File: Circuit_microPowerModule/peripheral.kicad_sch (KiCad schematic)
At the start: 25 parts, among them J4 Conn_01x08_Pin, J6 MikroBus

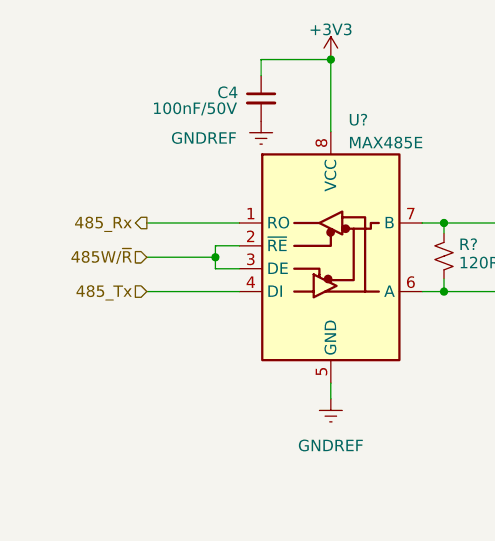
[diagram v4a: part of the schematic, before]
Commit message: define mcu pinout to mikrobus
update hw block diagram file type
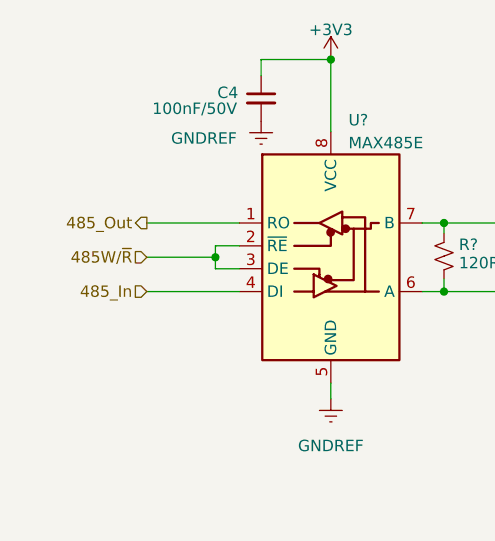
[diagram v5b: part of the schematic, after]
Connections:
- net 485_Rx renamed 485_Out
- net 485_Tx renamed 485_In
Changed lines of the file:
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@@
     (effects (font (size 1.27 1.27)) (justify right))
   )
-  (hierarchical_label "485_Tx" (shape input) (at 37.084 53.213 180) (fields_autoplaced)
+  (hierarchical_label "485_In" (shape input) (at 37.084 53.213 180) (fields_autoplaced)
     (effects (font (size 1.27 1.27)) (justify right))
   )
@@
     (effects (font (size 1.27 1.27)) (justify left))
   )
-  (hierarchical_label "485_Rx" (shape output) (at 37.084 45.593 180) (fields_autoplaced)
+  (hierarchical_label "485_Out" (shape output) (at 37.084 45.593 180) (fields_autoplaced)
     (effects (font (size 1.27 1.27)) (justify right))
   )

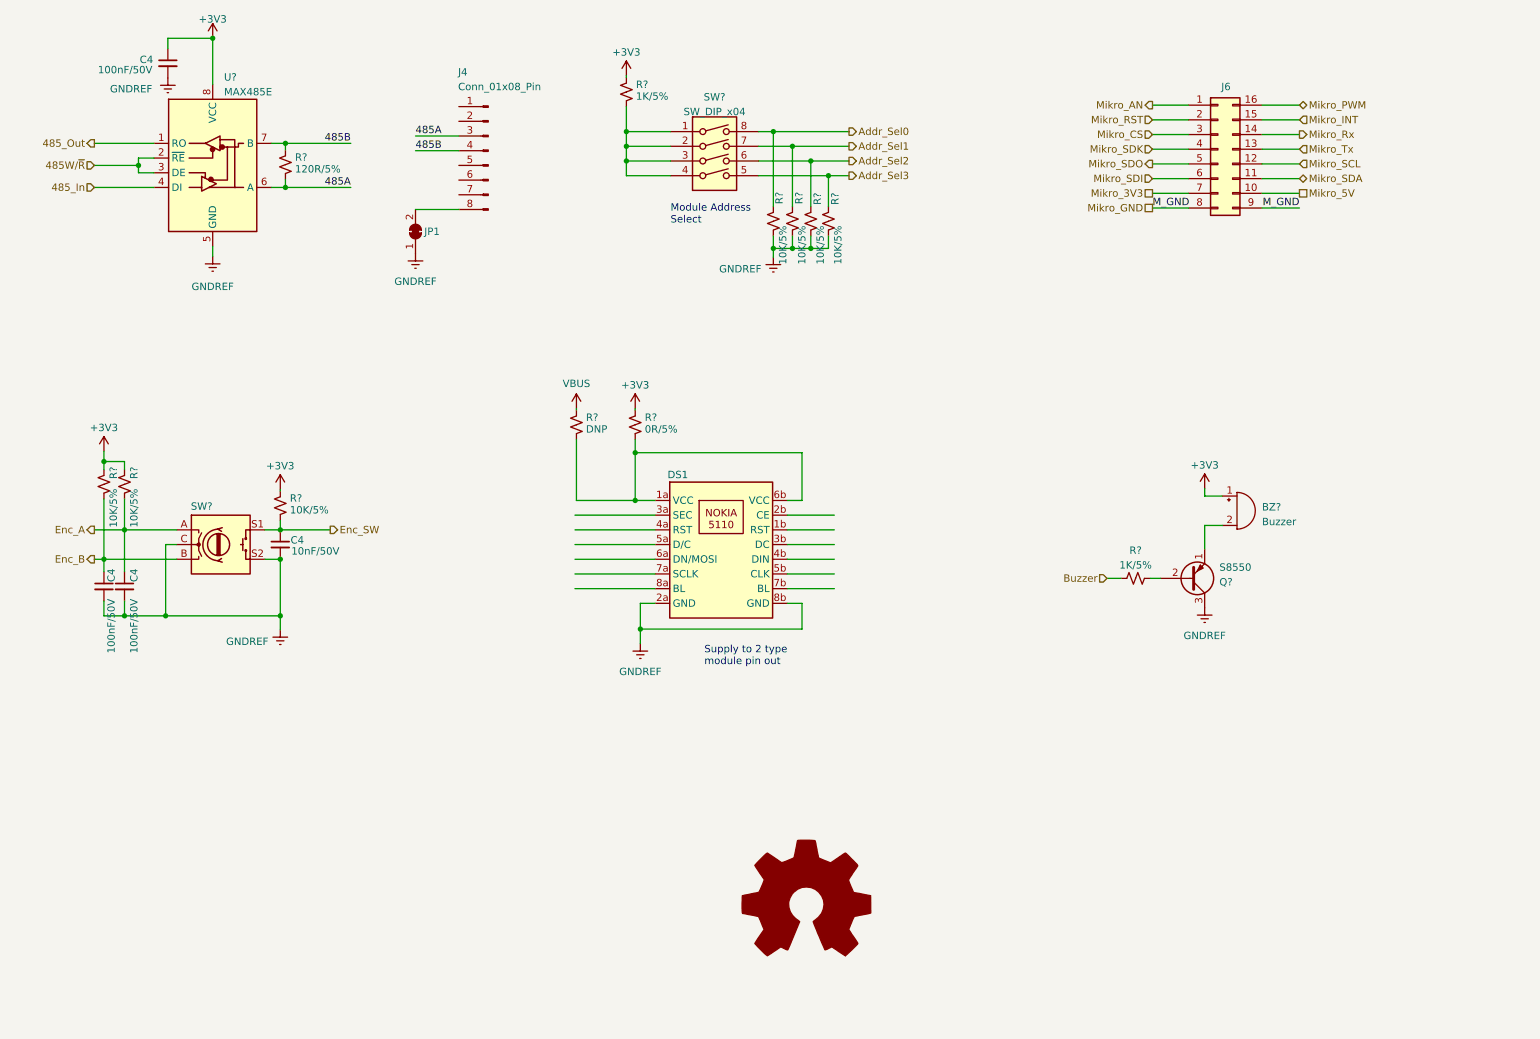
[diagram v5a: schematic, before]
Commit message: Completed microcontroller unit pin planning
update schematic
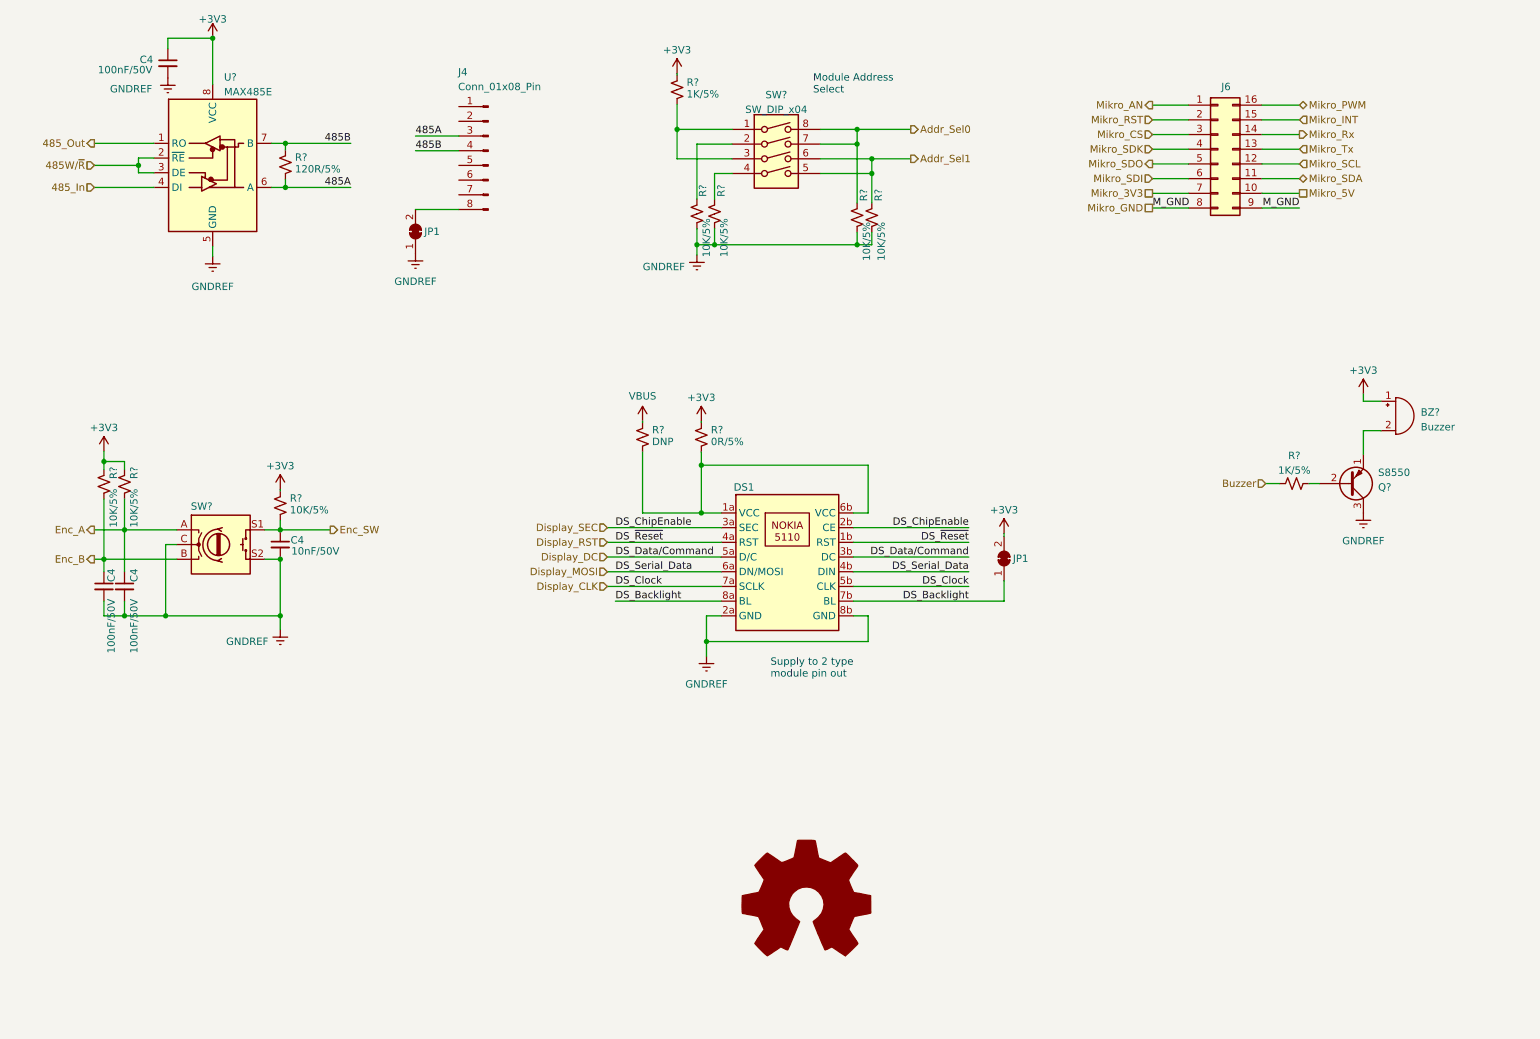
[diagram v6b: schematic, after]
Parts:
- added JP1: SolderJumper_2_Bridged, Jumper:SolderJumper-2_P1.3mm_Bridged_Pad1.0x1.5mm, symbol Jumper:SolderJumper_2_Bridged
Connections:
- net Addr_Sel3 is gone; now on net Addr_Sel1: R?.1, SW?.5
- net +3V3: now also JP1.2 (B)
- net Addr_Sel0: now also R?.1, SW?.7; no longer R?.1
- net Addr_Sel1: now also SW?.6; no longer R?.1, SW?.7
- net at R?.2, SW?.1, SW?.3: no longer SW?.2, SW?.4
- net Display_RST: now reaches DS1.1b (RST)
- net Display_RST: now also DS1.4a (RST)
- net Display_SEC: now reaches DS1.2b (CE)
- net Display_SEC: now also DS1.3a (SEC)
- net Display_DC: now reaches DS1.3b (DC)
- net Display_DC: now also DS1.5a (D/C)
- net Display_MOSI: now reaches DS1.4b (DIN)
- net Display_MOSI: now also DS1.6a (DN/MOSI)
- net Display_CLK: now reaches DS1.5b (CLK)
- net Display_CLK: now also DS1.7a (SCLK)
- net DS_Backlight: now reaches DS1.7b (BL)
- net DS_Backlight: now also DS1.8a (BL), JP1.1 (A)
- removed net Addr_Sel2: R?.1, SW?.6
- new net: R?.1, SW?.2
- new net: R?.1, SW?.4
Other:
- moved on the sheet: BZ?, DS1, Q?, R?, SW?

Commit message: change licenses
updated some footprint, create nokia 5110 lcd module pcb symbol, updated reademe
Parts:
- BZ?: footprint (none) -> Buzzer_Beeper:Buzzer_12x9.5RM7.6
- DS1: value ~ -> NOKIA 5110
- SW?: footprint (none) -> Rotary_Encoder:RotaryEncoder_Alps_EC11E-Switch_Vertical_H20mm
- SW?: footprint (none) -> Button_Switch_SMD:SW_DIP_SPSTx04_Slide_Copal_CHS-04B_W7.62mm_P1.27mm
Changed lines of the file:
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@@
       (effects (font (size 1.27 1.27)) hide)
     )
-    (property "Footprint" "" (at 55.118 110.871 0)
+    (property "Footprint" "Rotary_Encoder:RotaryEncoder_Alps_EC11E-Switch_Vertical_H20mm" (at 55.118 110.871 0)
       (effects (font (size 1.27 1.27)) hide)
     )
@@
       (effects (font (size 1.27 1.27)))
     )
-    (property "Footprint" "" (at 154.94 48.26 0)
+    (property "Footprint" "Button_Switch_SMD:SW_DIP_SPSTx04_Slide_Copal_CHS-04B_W7.62mm_P1.27mm" (at 154.94 48.26 0)
       (effects (font (size 1.27 1.27)) hide)
     )
@@
       (effects (font (size 1.27 1.27)) (justify left))
     )
-    (property "Value" "~" (at 147.955 106.299 0)
-      (effects (font (size 1.27 1.27)))
+    (property "Value" "NOKIA 5110" (at 158.115 105.029 0)
+      (effects (font (size 1.27 1.27)) hide)
     )
     (property "Footprint" "" (at 147.955 106.299 0)
@@
       (effects (font (size 1.27 1.27)) (justify left))
     )
-    (property "Footprint" "" (at 261.366 90.17 90)
-      (effects (font (size 1.27 1.27)) hide)
-    )
+    (property "Footprint" "Buzzer_Beeper:Buzzer_12x9.5RM7.6" (at 261.366 90.17 90)
+      (effects (font (size 1.27 1.27)) hide)
+    )

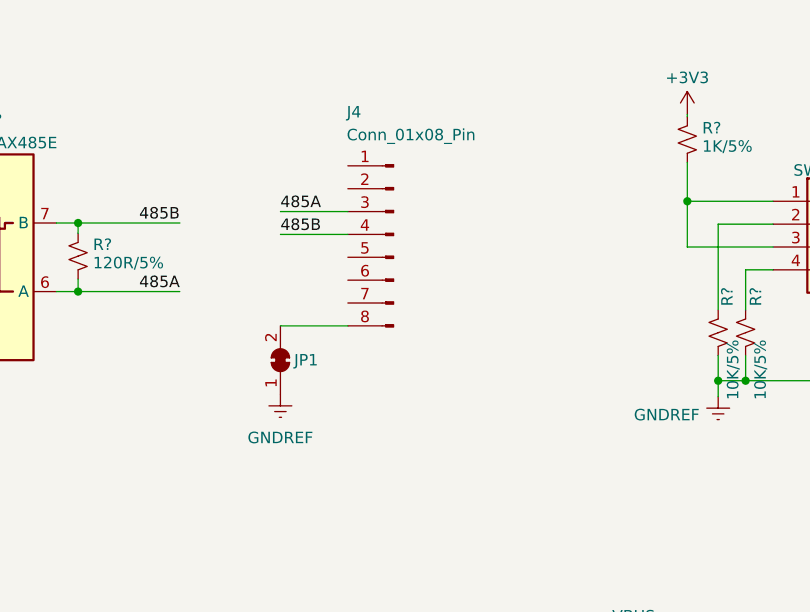
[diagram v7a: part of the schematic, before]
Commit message: update components footprint
check boost VR component, added Nokia 5110 LCD 3D module
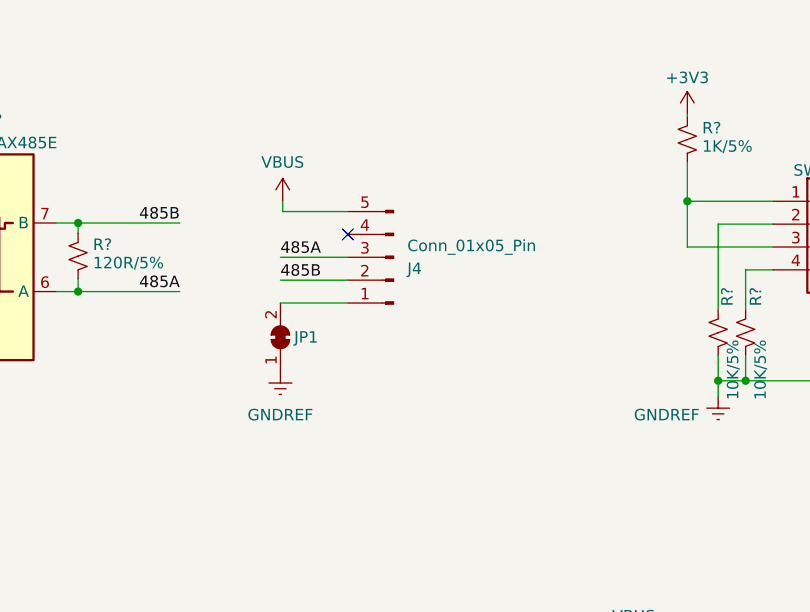
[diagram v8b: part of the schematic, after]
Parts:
- removed J4: Conn_01x08_Pin, symbol Connector:Conn_01x08_Pin
- added J4: Conn_01x05_Pin, Connector_PinHeader_2.54mm:PinHeader_1x05_P2.54mm_Vertical, symbol Connector:Conn_01x05_Pin
- C4: footprint (none) -> Capacitor_SMD:C_0603_1608Metric
- DS1: footprint (none) -> micro-PowerModule_Library:Nokia_5110_module
- J6: footprint (none) -> micro-PowerModule_Library:MIKROBUS_CONN
- U?: footprint (none) -> Package_SO:SOIC-8_3.9x4.9mm_P1.27mm
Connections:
- net 485A: now also J4.3 (Pin_3)
- net 485B: now also J4.2 (Pin_2)
- net VBUS: now also J4.5 (Pin_5)
- net at JP1.2 (B): now also J4.1 (Pin_1)
- no-connect marks 0 -> 1
